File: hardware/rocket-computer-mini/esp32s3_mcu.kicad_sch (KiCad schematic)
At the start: 40 parts, among them J5 Conn_01x04, SW3 R-667995, U11 GD5F2GQ5UEYIGR, U13 W25Q128JVSIQ, U14 479480001, U15 ESP32-S3RH2, U29 TPS22810DRVR, Y1 ABS07-32.768KHZ-T, Y2 ECS-400-10-37B2-CKY-TR

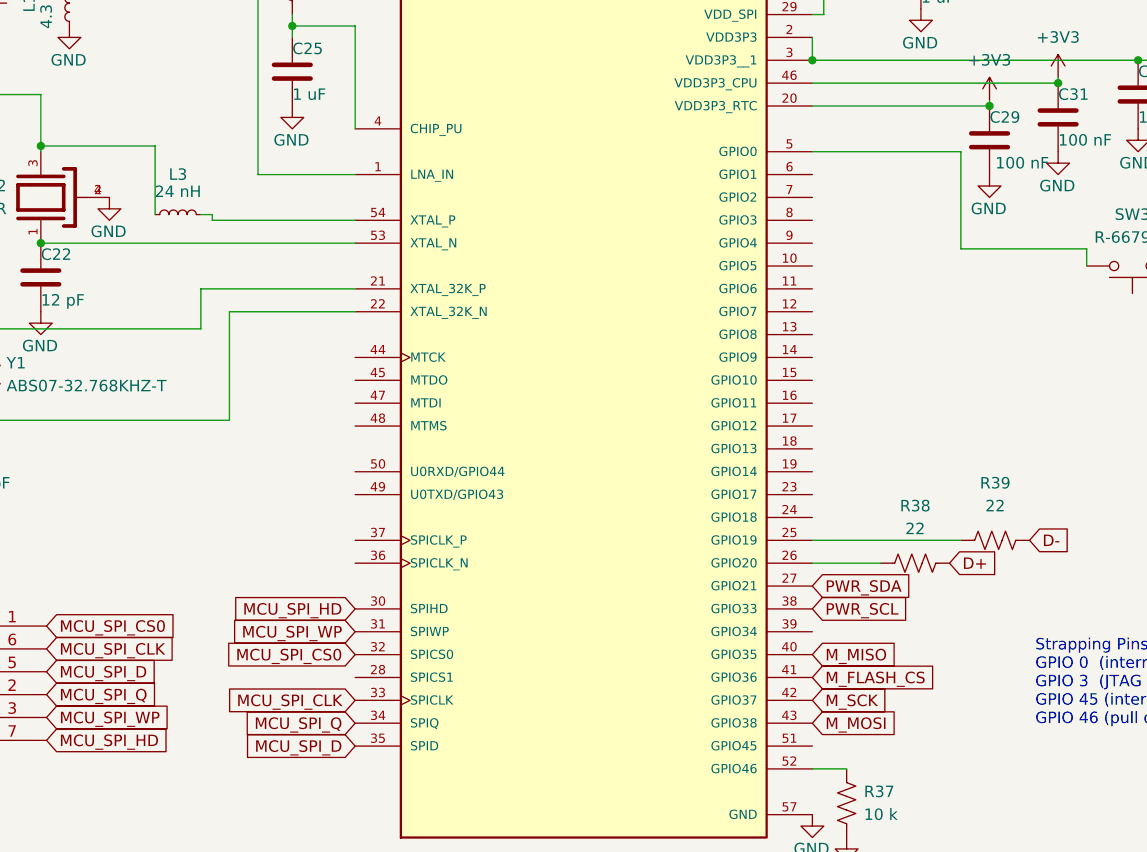
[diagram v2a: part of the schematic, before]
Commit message: hardware: wire the budgeted signals to the ESP32-S3
Connects all 24 pin-budget signals to the processor on the MCU sheet, by global
label at each pin anchor -- the pattern the sheet already uses for PWR_SDA,
M_SCK and the rest. Schematic only; the PCB is untouched.

Includes PERIPH_EN on GPIO3: one pin to power both the receiver and the radio,
per the decision to assume a single enable. GPIO3 is a strapping pad, which
suits an enable that idles low -- peripherals are then guaranteed off through
reset.

Verified: the netlist confirms all 24 signals reach U15. ERC 758 -> 720, the
drop being unconnected-pin violations clearing as pins get connected.

Seven named nets still have a single endpoint, each for a known reason, and all
are recorded in pin-budget.md: PERIPH_EN awaits its switch, the magnetometer
pair moves to the power-monitor I2C bus, GNSS_RXD2 was dropped by decision,
L_RXEN is the radio's floating receive-enable, and LoRa_RX/LoRa_TX belong to the
legacy connector the on-board radio replaces.

Also records a blocker found while tracing the power path. PERIPH_EN cannot yet
do its job: both existing load switches take their input from the battery rail,
not 3.3 V, because they were switching daughterboards that carried their own
regulators. The bare modules are 3.3 V parts -- the receiver is rated 2.55-3.6 V
-- so connecting either module to either switch output as wired today would
destroy it. Repointing one switch to +3V3 and removing the other is decided but
not implemented here.

Co-Authored-By: Claude Opus 5 <noreply@anthropic.com>
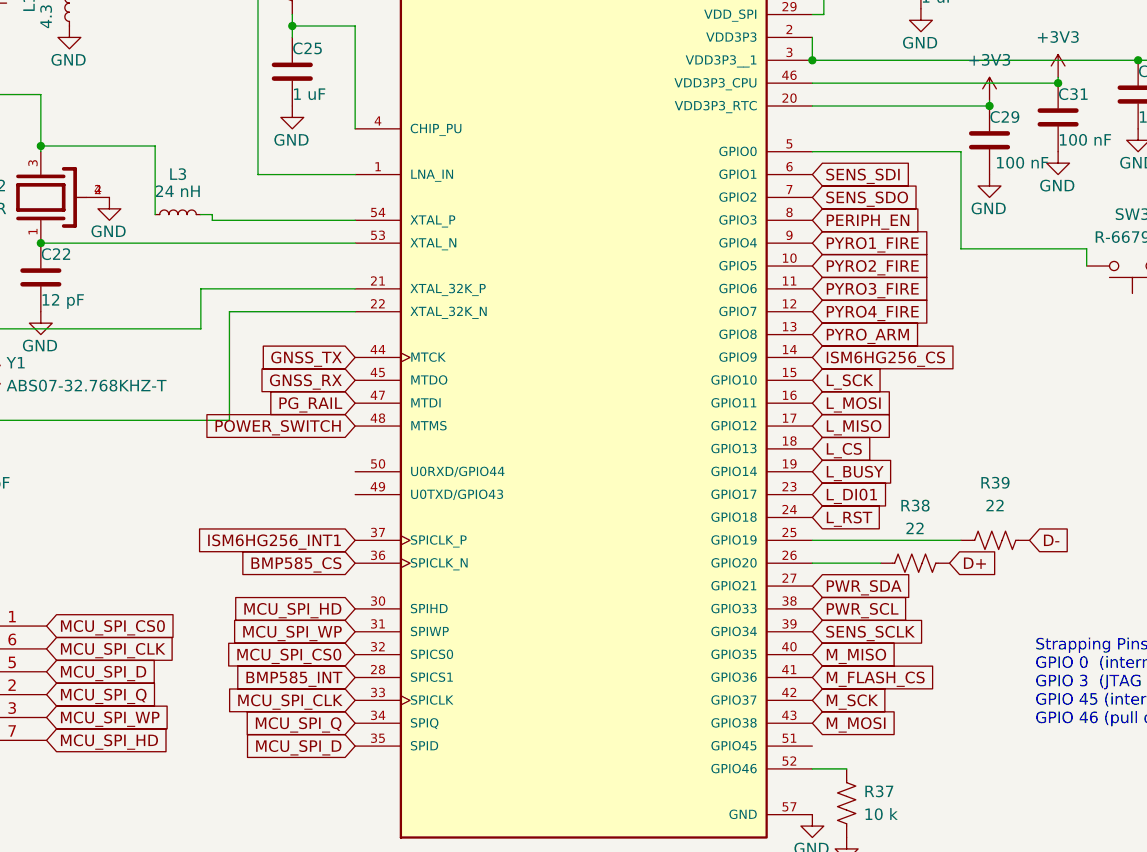
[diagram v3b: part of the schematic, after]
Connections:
- net BMP585_CS: now also U15.36 (SPICLK_N)
- net BMP585_INT: now also U15.28 (SPICS1)
- net GNSS_RX: now also U15.45 (MTDO)
- net GNSS_TX: now also U15.44 (MTCK)
- net ISM6HG256_CS: now also U15.14 (GPIO9)
- net ISM6HG256_INT1: now also U15.37 (SPICLK_P)
- net L_BUSY: now also U15.19 (GPIO14)
- net L_CS: now also U15.18 (GPIO13)
- net L_DI01: now also U15.23 (GPIO17)
- net L_MISO: now also U15.17 (GPIO12)
- net L_MOSI: now also U15.16 (GPIO11)
- net L_RST: now also U15.24 (GPIO18)
- net L_SCK: now also U15.15 (GPIO10)
- net PYRO1_FIRE: now also U15.9 (GPIO4)
- net PYRO2_FIRE: now also U15.10 (GPIO5)
- net PYRO3_FIRE: now also U15.11 (GPIO6)
- net PYRO4_FIRE: now also U15.12 (GPIO7)
- net PYRO_ARM: now also U15.13 (GPIO8)
- net SENS_SCLK: now also U15.39 (GPIO34)
- net SENS_SDI: now also U15.6 (GPIO1)
- net SENS_SDO: now also U15.7 (GPIO2)
- net PG_RAIL: now reaches U15.47 (MTDI)
- net POWER_SWITCH: now reaches U15.48 (MTMS)
- net PERIPH_EN: now reaches U15.8 (GPIO3)

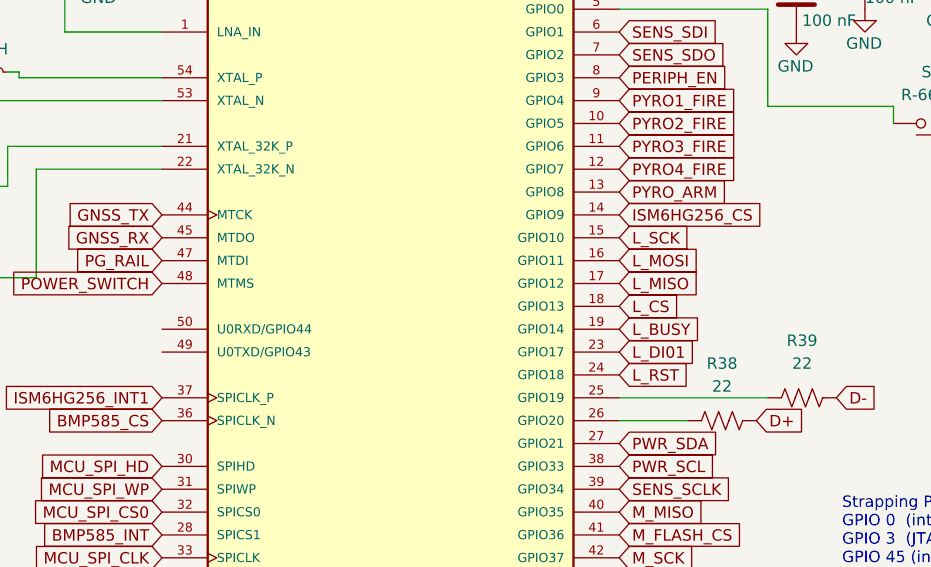
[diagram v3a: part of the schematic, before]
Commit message: hardware: radio joins the memory SPI bus, continuity sensing restored
Two changes that turned out to be the same change.

The radio moves onto the memory SPI bus -- clock, data-in and data-out shared
with the NAND, chip selects kept separate, which is what a bus is for. That
frees three processor pins for no new parts, and those pins go straight to pyro
continuity sensing, which until now reached nothing at all.

Continuity had been quietly lost. Those four nets went to the removed processor
and kept two nodes each -- a sense resistor and a clamp -- so they never showed
up in the single-endpoint sweep used to track what still needed rehoming. The
front end was intact the whole time; only the readout was missing. A board that
cannot check continuity can arm and fire into an open circuit and report nothing
wrong.

Which two devices share matters, and it is a latency question rather than a
bandwidth one -- there is large bandwidth margin either way. Memory moves in
page-sized bursts at 40 MHz that block the bus for hundreds of microseconds;
sensors are read per-sample on data-ready rather than batched through a FIFO, so
any bus delay lands directly as jitter on the sample timebase, and those samples
get integrated. The radio sends one small packet twice a second. Pairing memory
with the radio costs nothing; pairing it with the sensors would have put the
most latency-sensitive device behind the longest transactions.

This does split sensors and memory across hosts, which is not how the V7
firmware had them -- but this board has no firmware map yet, so the host
assignment is being written from scratch regardless.

The fourth continuity channel sits on GPIO44, spending the console receive line,
rather than the spare GPIO45. GPIO45 is sampled at reset to set the flash rail
voltage, and a continuity input's boot level depends on whether an igniter is
connected, which the design does not control -- an armed channel could hold that
pad high and stop the board booting. GPIO43 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
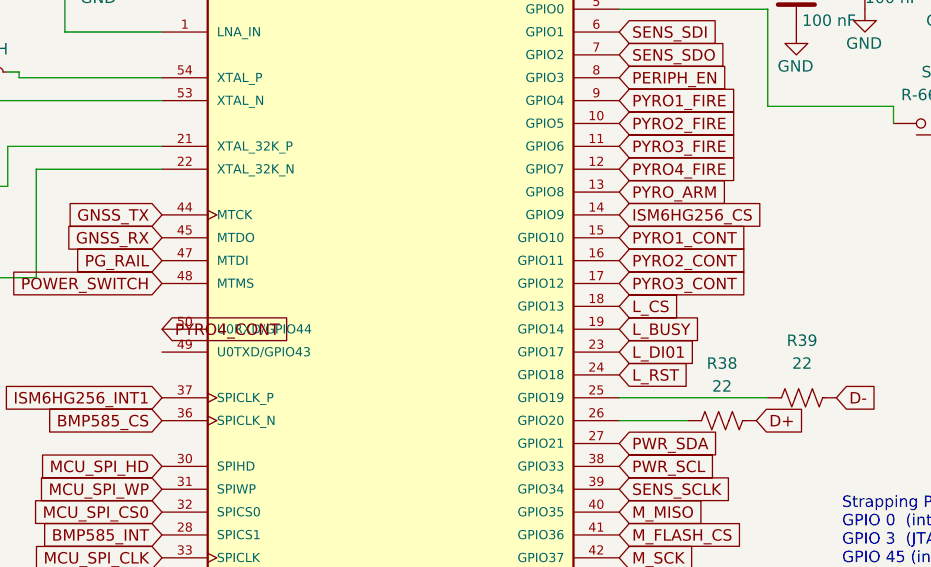
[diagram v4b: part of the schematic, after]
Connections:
- net L_MISO: no longer U15.17 (GPIO12)
- net L_MOSI: no longer U15.16 (GPIO11)
- net L_SCK: no longer U15.15 (GPIO10)
- net PYRO1_CONT: now also U15.15 (GPIO10)
- net PYRO2_CONT: now also U15.16 (GPIO11)
- net PYRO3_CONT: now also U15.17 (GPIO12)
- net PYRO4_CONT: now also U15.50 (U0RXD/GPIO44)
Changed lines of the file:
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@@
 		)
 	)
-	(global_label "L_SCK"
+	(global_label "PYRO1_CONT"
 		(shape input)
 		(at 212.725 76.2 0)
@@
 		)
 	)
-	(global_label "L_MOSI"
+	(global_label "PYRO2_CONT"
 		(shape input)
 		(at 212.725 78.74000000000001 0)
@@
 		)
 	)
-	(global_label "L_MISO"
+	(global_label "PYRO3_CONT"
 		(shape input)
 		(at 212.725 81.28 0)
@@
 			)
 		)
+	)
+	(global_label "PYRO4_CONT"
+		(shape input)
+		(at 161.92499999999998 86.36 0)
+		(fields_autoplaced yes)
+		(effects
+			(font
+				(size 1.27 1.27)
+			)
+			(justify left)
+		)
+		(property "Intersheetrefs" "${INTERSHEET_REFS}"
+			(at 173.4373 86.36 0)
+			(hide yes)
+			(show_name no)
+			(do_not_autoplace no)
+			(effects
+				(font
+					(size 1.27 1.27)
+				)
+				(justify left)
+			)
+		)

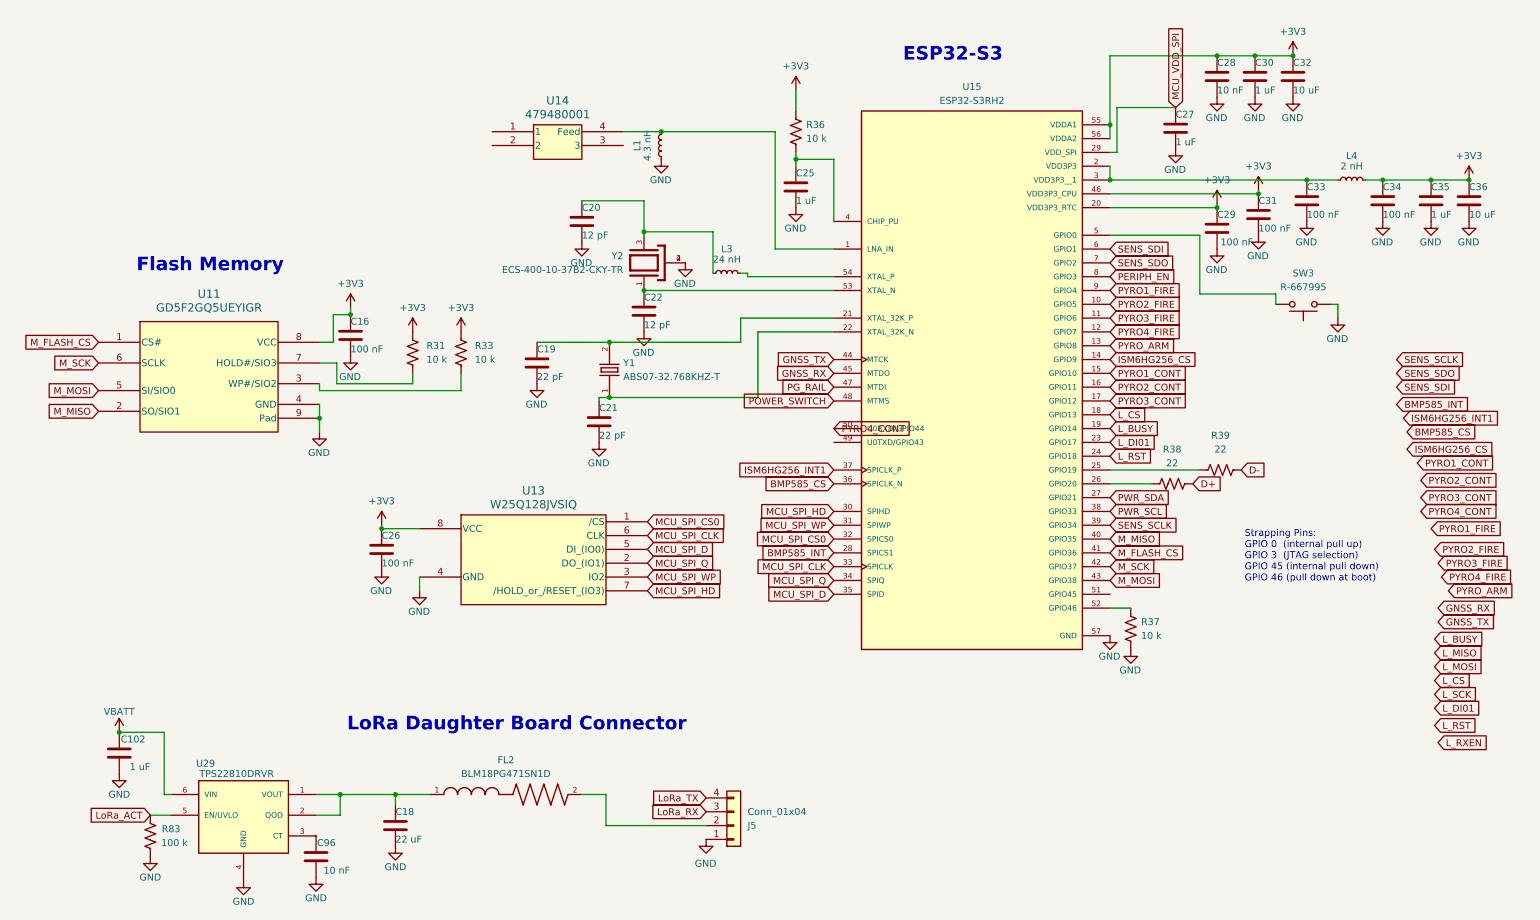
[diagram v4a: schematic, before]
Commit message: hardware: move two signals off the risky processor pads
Audits every special-function pin the assignment touches and moves the two that
were not defensible, using pads freed by dropping power-good and the peripheral
enable.

BMP585_INT leaves GPIO26 for GPIO41. GPIO26 is the quad PSRAM chip select, and
the evidence that this part has no PSRAM only covers the octal variety -- the V7
board drove GPIO34-38 on hardware that was built and flown, which rules out
octal but says nothing about quad, and quad uses exactly GPIO26. Rather than
resolve the package suffix, the pin is now simply unused.

PYRO4_CONT leaves GPIO44 for GPIO42, returning the full serial console. A
console that works from first power-on with no adapter is worth more during
bring-up than the JTAG pads it costs.

Everything else checks out. GPIO27-32 carry the external boot flash and are used
as intended. GPIO33-37 and GPIO47/48 serve octal PSRAM only, which the V7
hardware proves is absent. GPIO39-42 are ordinary GPIO once debug is given up.
GPIO3 drives a switch enable and its pulldown holds it low through reset, which
is the behaviour that pad wants anyway.

GPIO45 stays unused on purpose: it sets the flash rail voltage at reset, and any
signal whose boot level the design does not control can stop the board booting.

Four pads now free -- GPIO26, GPIO43, GPIO44, GPIO45 -- and both hazardous ones
are among them. Schematic only.

Co-Authored-By: Claude Opus 5 <noreply@anthropic.com>
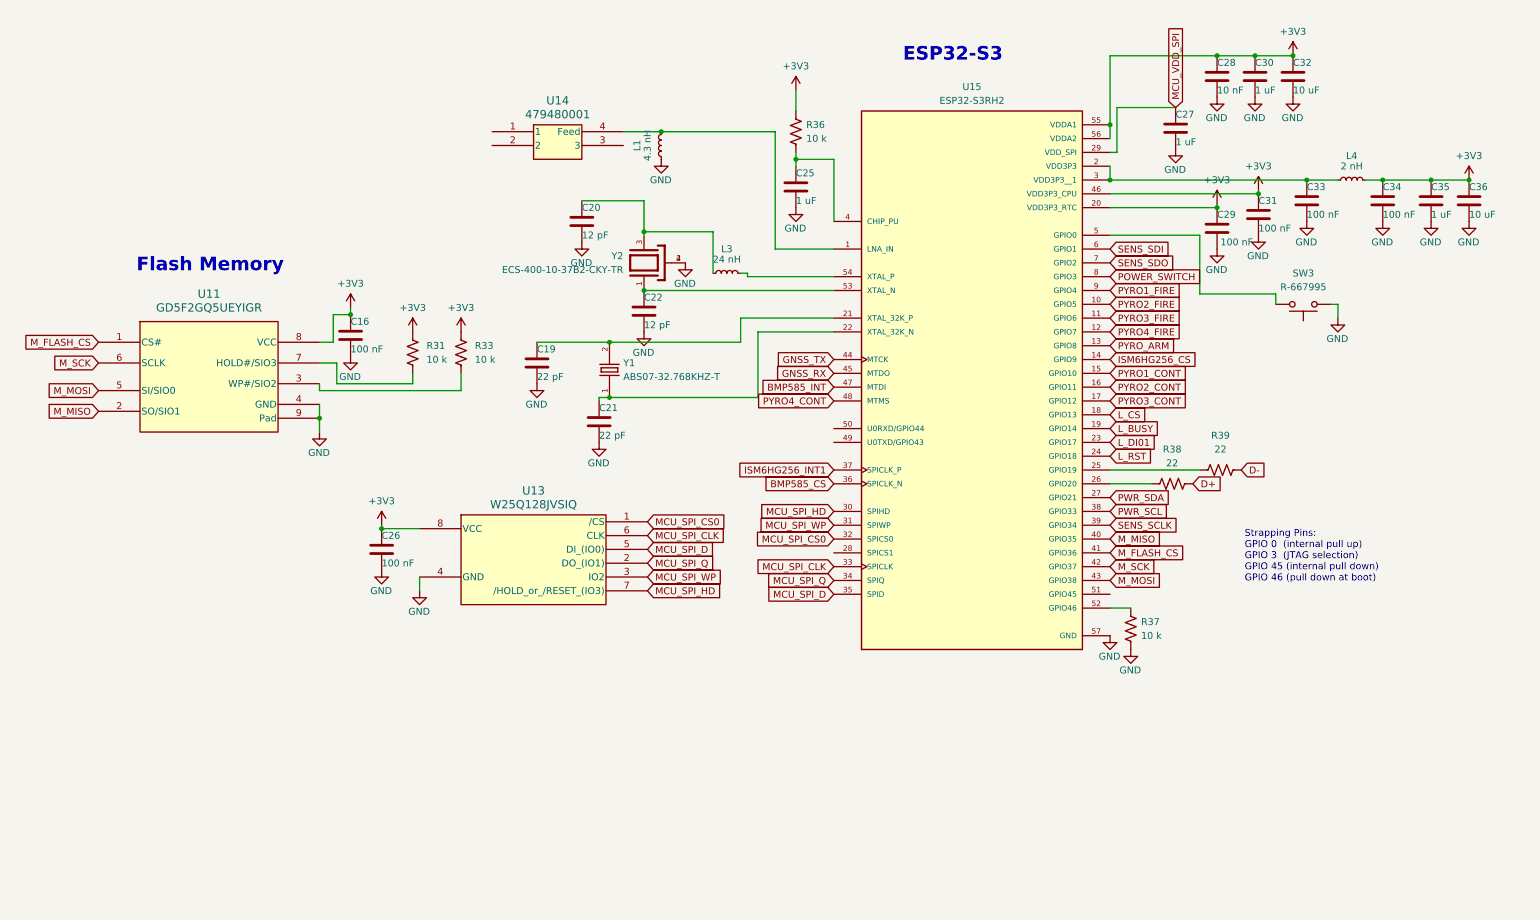
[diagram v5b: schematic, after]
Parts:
- removed C102: 1 uF, Capacitor_SMD:C_0402_1005Metric, symbol Device:C
- removed C18: 22 uF, Capacitor_SMD:C_0805_2012Metric, symbol Device:C
- removed C96: 10 nF, Capacitor_SMD:C_0402_1005Metric, symbol Device:C
- removed FL2: BLM18PG471SN1D, Footprints:BEADC1608X95N, symbol Custom:BLM18PG471SN1D
- removed J5: Conn_01x04, Connector_JST:JST_SH_BM04B-SRSS-TB_1x04-1MP_P1.00mm_Vertical, symbol Connector_Generic:Conn_01x04
- removed R83: 100 k, Resistor_SMD:R_0402_1005Metric, symbol Device:R_US
- removed U29: TPS22810DRVR, Footprints:SON65P200X200X80-7N, symbol Custom:TPS22810DRVR
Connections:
- net PERIPH_EN is gone; now on net POWER_SWITCH: U15.8 (GPIO3)
- net PG_RAIL is gone; now on net BMP585_INT: U15.47 (MTDI)
- net BMP585_INT: no longer U15.28 (SPICS1)
- net POWER_SWITCH: no longer U15.48 (MTMS)
- net PYRO4_CONT: now also U15.48 (MTMS); no longer U15.50 (U0RXD/GPIO44)
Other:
- note removed: "LoRa Daughter Board Connector"

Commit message: hardware: magnetometer onto the shared I2C bus, NAND to the switched rail, radio RX-enable wired
Three connectivity fixes and one bus correction.

The magnetometer joins the power monitor on one I2C bus, renamed SEN_SCL /
SEN_SDA, with both parts and the processor on it. The rename initially stranded
the bus pull-ups on the old net names, leaving an open-drain bus with nothing to
pull it high and both devices unusable; R67 and R69 are now back on the live
nets.

The NAND moves to the switched rail. That closes the split introduced when the
radio moved to switched power while the NAND stayed always-on -- a powered
device driving a bus into unpowered silicon. Both bus slaves now share one
domain and the only always-on device is the processor, whose pins are inputs
after reset (datasheet Table 2-1), so nothing drives into a dead rail. The cost
is that the log memory now drops out whenever the peripheral rail is cycled, and
NAND can lose a block if power goes during program or erase -- firmware should
close the log before any deliberate cycle.

The radio's receive-enable reaches GPIO44. This matches what both existing radio
boards do rather than the inverter previously suggested here: the vendor's split
shorts DIO2 to TXEN on the board and brings only the RX half to a processor pin.
DIO3 stays floating, as it must -- the module has its own passive crystal and
must never be configured for a DIO3-powered TCXO.

Firmware already carries rxen_pin in the radio config and both the daughterboard
and base-station projects set it, but the out-computer project defines no
LORA_RXEN_PIN, so this pin does nothing until the board map declares it. The
base-station sources record this same defect having shipped once already --
"was defined but never driven, RXEN floated in RX".

Two pads remain: GPIO26, which the in-package PSRAM owns and cannot be used, and
GPIO43, kept free so the boot ROM can still print. ERC 637 -> 629.

Co-Authored-By: Claude Opus 5 <noreply@anthropic.com>
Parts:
- added D8: White, LED_SMD:LED_0402_1005Metric, symbol Device:LED
- added R68: 10 k, Resistor_SMD:R_0402_1005Metric, symbol Device:R_US
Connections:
- net +3V3: no longer C16.1, R31.2, R33.2, U11.8 (VCC)
- net GND: now also D8.1 (K)
- net L_RXEN: now reaches U15.50 (U0RXD/GPIO44)
- net at U15.51 (GPIO45): now also R68.1
- net PWR_SCL renamed SEN_SCL
- net PWR_SDA renamed SEN_SDA
- new net: D8.2 (A), R68.2
- new net V_MCU_SWTCH: C16.1, R31.2, R33.2, U11.8 (VCC)
